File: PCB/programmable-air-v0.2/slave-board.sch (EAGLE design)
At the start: 20 parts, among them Q1 600mA/40V, Q2 600mA/40V, Q3 600mA/40V

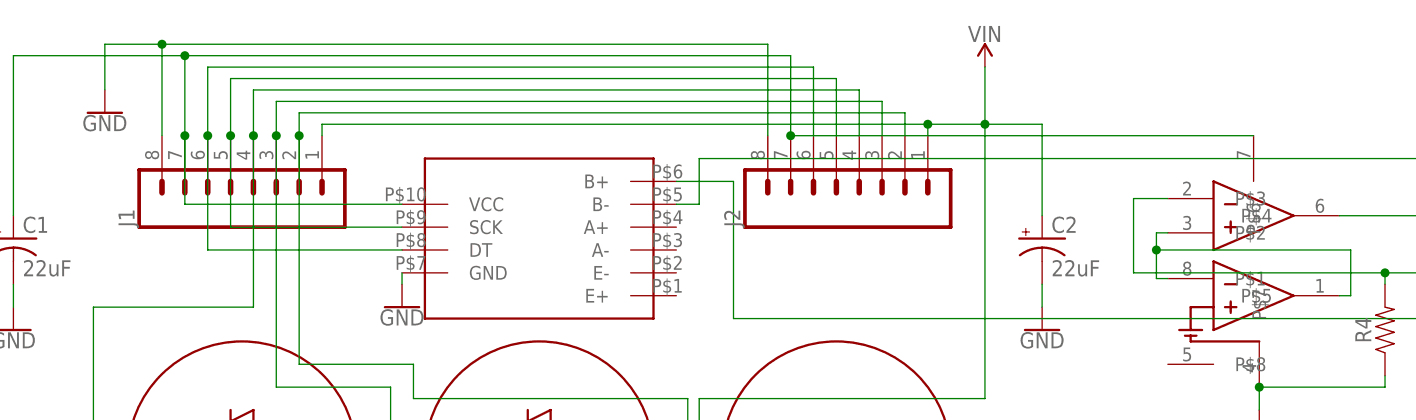
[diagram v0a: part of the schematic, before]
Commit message: PCB v0.2 slave board ready
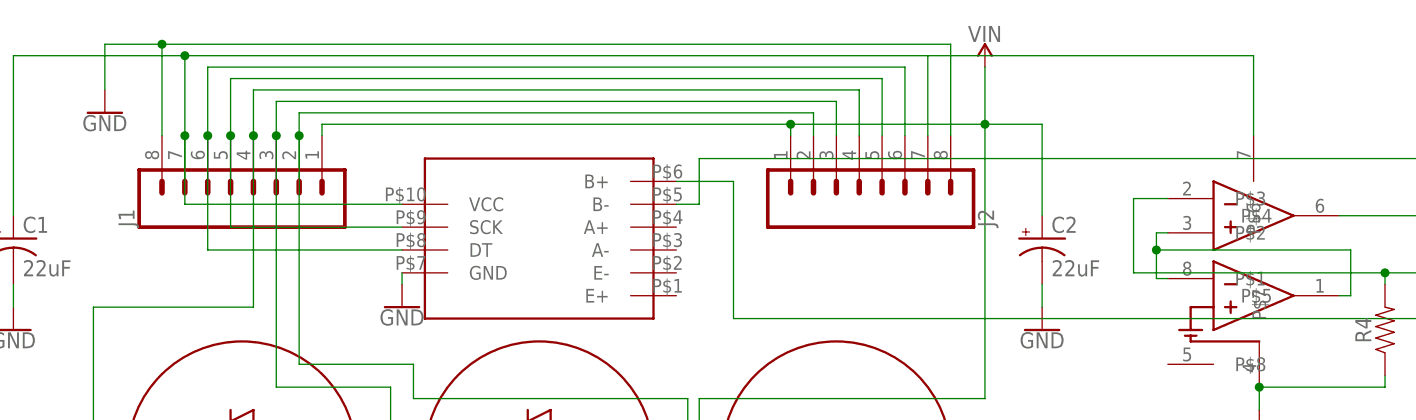
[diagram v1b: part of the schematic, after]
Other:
- moved on the sheet: J2
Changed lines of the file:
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@@
 <?xml version="1.0" encoding="utf-8"?>
 <!DOCTYPE eagle SYSTEM "eagle.dtd">
-<eagle version="8.2.1">
+<eagle version="8.7.0">
 <drawing>
 <settings>
 <setting alwaysvectorfont="no"/>
+<setting keepoldvectorfont="yes"/>
 <setting verticaltext="up"/>
 </settings>
-<grid distance="0.1" unitdist="inch" unit="inch" style="lines" multiple="1" display="no" altdistance="0.01" altunitdist="inch" altunit="inch"/>
+<grid distance="0.05" unitdist="inch" unit="inch" style="lines" multiple="1" display="no" altdistance="0.01" altunitdist="inch" altunit="inch"/>
 <layers>
 <layer number="1" name="Top" color="4" fill="1" visible="no" active="no"/>
@@
 <instance part="U$4" gate="G$1" x="33.02" y="-10.16"/>
 <instance part="J1" gate="G$1" x="-31.75" y="20.32" rot="R90"/>
-<instance part="J2" gate="G$1" x="35.56" y="20.32" rot="R90"/>
+<instance part="J2" gate="G$1" x="35.56" y="20.32" rot="MR90"/>
 <instance part="Q1" gate="G$1" x="-35.56" y="-16.51"/>
 <instance part="Q2" gate="G$1" x="-2.54" y="-16.51"/>
@@
 <net name="N$5" class="0">
 <segment>
-<pinref part="J2" gate="G$1" pin="2"/>
-<wire x1="40.64" y1="25.4" x2="40.64" y2="27.94" width="0.1524" layer="91"/>
-<wire x1="40.64" y1="27.94" x2="-26.67" y2="27.94" width="0.1524" layer="91"/>
 <pinref part="J1" gate="G$1" pin="2"/>
 <wire x1="-26.67" y1="27.94" x2="-26.67" y2="25.4" width="0.1524" layer="91"/>
@@
 <wire x1="-26.67" y1="0" x2="-26.67" y2="25.4" width="0.1524" layer="91"/>
 <junction x="-26.67" y="25.4"/>
+<pinref part="J2" gate="G$1" pin="2"/>
+<wire x1="30.48" y1="25.4" x2="30.48" y2="27.94" width="0.1524" layer="91"/>
+<wire x1="30.48" y1="27.94" x2="-26.67" y2="27.94" width="0.1524" layer="91"/>
 </segment>
 </net>
@@
 <pinref part="J1" gate="G$1" pin="3"/>
 <wire x1="-29.21" y1="25.4" x2="-29.21" y2="29.21" width="0.1524" layer="91"/>
-<wire x1="-29.21" y1="29.21" x2="38.1" y2="29.21" width="0.1524" layer="91"/>
-<pinref part="J2" gate="G$1" pin="3"/>
-<wire x1="38.1" y1="29.21" x2="38.1" y2="25.4" width="0.1524" layer="91"/>
 <wire x1="-29.21" y1="25.4" x2="-29.21" y2="-2.54" width="0.1524" layer="91"/>
 <wire x1="-29.21" y1="-2.54" x2="-16.51" y2="-2.54" width="0.1524" layer="91"/>
@@
 <wire x1="-16.51" y1="-2.54" x2="-16.51" y2="-16.51" width="0.1524" layer="91"/>
 <junction x="-29.21" y="25.4"/>
+<wire x1="-29.21" y1="29.21" x2="33.02" y2="29.21" width="0.1524" layer="91"/>
+<pinref part="J2" gate="G$1" pin="3"/>
+<wire x1="33.02" y1="29.21" x2="33.02" y2="25.4" width="0.1524" layer="91"/>
 </segment>
 </net>
 <net name="N$12" class="0">
 <segment>
-<pinref part="J2" gate="G$1" pin="4"/>
-<wire x1="35.56" y1="25.4" x2="35.56" y2="30.48" width="0.1524" layer="91"/>
-<wire x1="35.56" y1="30.48" x2="-31.75" y2="30.48" width="0.1524" layer="91"/>
 <pinref part="J1" gate="G$1" pin="4"/>
 <wire x1="-31.75" y1="30.48" x2="-31.75" y2="25.4" width="0.1524" layer="91"/>
@@
 <wire x1="-31.75" y1="6.35" x2="-31.75" y2="25.4" width="0.1524" layer="91"/>
 <junction x="-31.75" y="25.4"/>
+<pinref part="J2" gate="G$1" pin="4"/>
+<wire x1="35.56" y1="25.4" x2="35.56" y2="30.48" width="0.1524" layer="91"/>
+<wire x1="35.56" y1="30.48" x2="-31.75" y2="30.48" width="0.1524" layer="91"/>
 </segment>
 </net>
@@
 <pinref part="J1" gate="G$1" pin="5"/>
 <wire x1="-34.29" y1="25.4" x2="-34.29" y2="31.75" width="0.1524" layer="91"/>
-<wire x1="-34.29" y1="31.75" x2="33.02" y2="31.75" width="0.1524" layer="91"/>
-<pinref part="J2" gate="G$1" pin="5"/>
-<wire x1="33.02" y1="31.75" x2="33.02" y2="25.4" width="0.1524" layer="91"/>
 <pinref part="U$1" gate="G$1" pin="SCK"/>
 <wire x1="-34.29" y1="25.4" x2="-34.29" y2="15.24" width="0.1524" layer="91"/>
 <wire x1="-34.29" y1="15.24" x2="-15.24" y2="15.24" width="0.1524" layer="91"/>
 <junction x="-34.29" y="25.4"/>
+<pinref part="J2" gate="G$1" pin="5"/>
+<wire x1="-34.29" y1="31.75" x2="38.1" y2="31.75" width="0.1524" layer="91"/>
+<wire x1="38.1" y1="31.75" x2="38.1" y2="25.4" width="0.1524" layer="91"/>
 </segment>
 </net>
 <net name="N$14" class="0">
 <segment>
-<pinref part="J2" gate="G$1" pin="6"/>
-<wire x1="30.48" y1="25.4" x2="30.48" y2="33.02" width="0.1524" layer="91"/>
-<wire x1="30.48" y1="33.02" x2="-36.83" y2="33.02" width="0.1524" layer="91"/>
 <pinref part="J1" gate="G$1" pin="6"/>
 <wire x1="-36.83" y1="33.02" x2="-36.83" y2="25.4" width="0.1524" layer="91"/>
@@
 <wire x1="-36.83" y1="12.7" x2="-36.83" y2="25.4" width="0.1524" layer="91"/>
 <junction x="-36.83" y="25.4"/>
+<pinref part="J2" gate="G$1" pin="6"/>
+<wire x1="40.64" y1="25.4" x2="40.64" y2="33.02" width="0.1524" layer="91"/>
+<wire x1="40.64" y1="33.02" x2="-36.83" y2="33.02" width="0.1524" layer="91"/>
 </segment>
 </net>
@@
 <pinref part="J1" gate="G$1" pin="7"/>
 <wire x1="-39.37" y1="25.4" x2="-39.37" y2="34.29" width="0.1524" layer="91"/>
-<wire x1="-39.37" y1="34.29" x2="27.94" y2="34.29" width="0.1524" layer="91"/>
-<pinref part="J2" gate="G$1" pin="7"/>
-<wire x1="27.94" y1="34.29" x2="27.94" y2="25.4" width="0.1524" layer="91"/>
 <pinref part="U$1" gate="G$1" pin="VCC"/>
 <wire x1="-39.37" y1="25.4" x2="-39.37" y2="17.78" width="0.1524" layer="91"/>
@@
 <wire x1="-39.37" y1="34.29" x2="-58.42" y2="34.29" width="0.1524" layer="91"/>
 <wire x1="-58.42" y1="34.29" x2="-58.42" y2="16.51" width="0.1524" layer="91"/>
+<junction x="-39.37" y="25.4"/>
+<pinref part="J2" gate="G$1" pin="7"/>
+<wire x1="-39.37" y1="34.29" x2="43.18" y2="34.29" width="0.1524" layer="91"/>
 <junction x="-39.37" y="34.29"/>
-<junction x="-39.37" y="25.4"/>
+<wire x1="43.18" y1="34.29" x2="43.18" y2="25.4" width="0.1524" layer="91"/>
 <pinref part="U$9" gate="G$1" pin="P$6"/>
-<wire x1="27.94" y1="25.4" x2="79.375" y2="25.4" width="0.1524" layer="91"/>
-<junction x="27.94" y="25.4"/>
+<wire x1="43.18" y1="34.29" x2="79.375" y2="34.29" width="0.1524" layer="91"/>
+<wire x1="79.375" y1="34.29" x2="79.375" y2="25.4" width="0.1524" layer="91"/>
 </segment>
 </net>
@@
 <pinref part="J1" gate="G$1" pin="1"/>
 <wire x1="-24.13" y1="25.4" x2="-24.13" y2="26.67" width="0.1524" layer="91"/>
-<pinref part="J2" gate="G$1" pin="1"/>
-<wire x1="-24.13" y1="26.67" x2="43.18" y2="26.67" width="0.1524" layer="91"/>
-<wire x1="43.18" y1="26.67" x2="43.18" y2="25.4" width="0.1524" layer="91"/>
+<wire x1="-24.13" y1="26.67" x2="27.94" y2="26.67" width="0.1524" layer="91"/>
 <pinref part="SUPPLY1" gate="G$1" pin="VIN"/>
-<wire x1="43.18" y1="26.67" x2="49.53" y2="26.67" width="0.1524" layer="91"/>
+<wire x1="27.94" y1="26.67" x2="49.53" y2="26.67" width="0.1524" layer="91"/>
 <wire x1="49.53" y1="26.67" x2="49.53" y2="33.02" width="0.1524" layer="91"/>
 <pinref part="U$2" gate="G$1" pin="P$1"/>
@@
 <junction x="17.78" y="-7.62"/>
 <junction x="-15.24" y="-8.89"/>
-<junction x="43.18" y="26.67"/>
 <junction x="17.78" y="-8.89"/>
 <pinref part="C2" gate="G$1" pin="+"/>
 <wire x1="55.88" y1="16.51" x2="55.88" y2="26.67" width="0.1524" layer="91"/>
 <wire x1="49.53" y1="26.67" x2="55.88" y2="26.67" width="0.1524" layer="91"/>
+<pinref part="J2" gate="G$1" pin="1"/>
+<wire x1="27.94" y1="26.67" x2="27.94" y2="25.4" width="0.1524" layer="91"/>
+<junction x="27.94" y="26.67"/>
 </segment>
 </net>
@@
 <wire x1="-48.26" y1="35.56" x2="-41.91" y2="35.56" width="0.1524" layer="91"/>
 <pinref part="J1" gate="G$1" pin="8"/>
+<wire x1="-41.91" y1="35.56" x2="-41.91" y2="25.4" width="0.1524" layer="91"/>
 <pinref part="J2" gate="G$1" pin="8"/>
-<wire x1="25.4" y1="25.4" x2="25.4" y2="35.56" width="0.1524" layer="91"/>
-<wire x1="25.4" y1="35.56" x2="-41.91" y2="35.56" width="0.1524" layer="91"/>
-<wire x1="-41.91" y1="35.56" x2="-41.91" y2="25.4" width="0.1524" layer="91"/>
+<wire x1="45.72" y1="25.4" x2="45.72" y2="35.56" width="0.1524" layer="91"/>
+<wire x1="45.72" y1="35.56" x2="-41.91" y2="35.56" width="0.1524" layer="91"/>
 <junction x="-41.91" y="35.56"/>
 </segment>

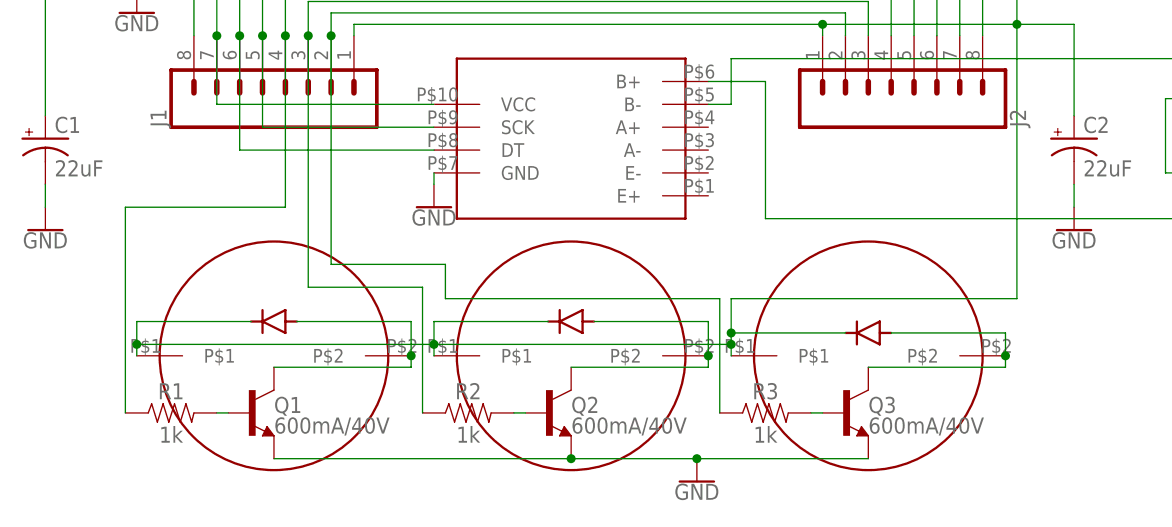
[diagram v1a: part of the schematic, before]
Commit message: Minor fixes to slave PCB after assembly. Started work on test code for PCB v0.2
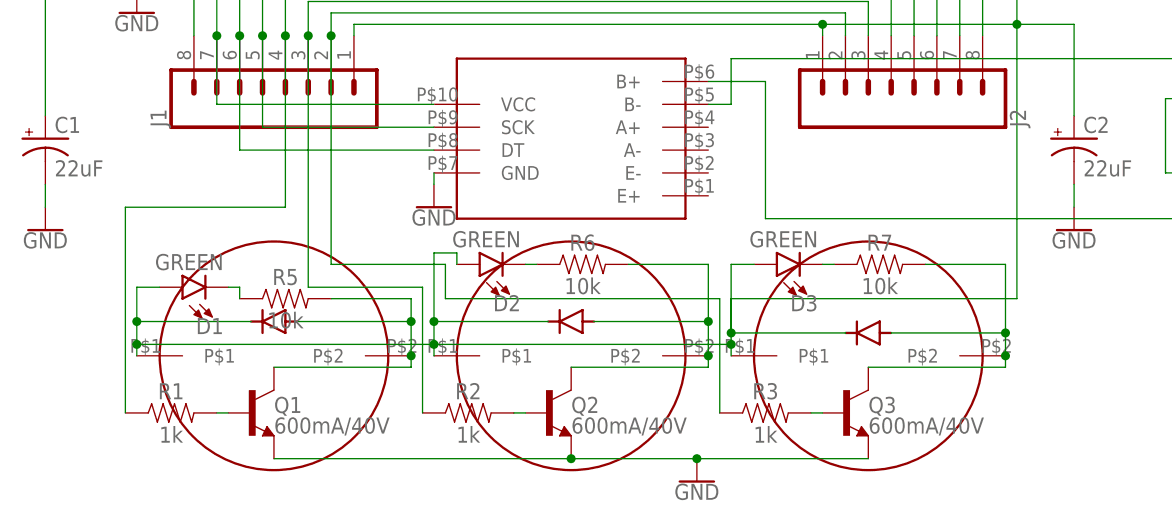
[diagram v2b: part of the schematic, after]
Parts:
- added D1, D2, D3: GREEN, SparkFun-LED:LED-GREEN0603
- added R5, R6, R7: 10k, SparkFun-Resistors:10KOHM-0603-1/10W-1%
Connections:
- new net N$11: D2.C, R6.1
- new net N$18: D1.C, R5.1
- new net N$6: D3.C, R7.1
- net N$7: now also R7.2
- net N$8: now also R6.2
- net N$9: now also R5.2
- net VIN: now also D1.A, D2.A, D3.A
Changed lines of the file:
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@@
 <part name="R4" library="SparkFun-Resistors" deviceset="RESISTOR" device="AXIAL-0.3" value=" "/>
 <part name="GND6" library="SparkFun-PowerSymbols" deviceset="GND" device=""/>
+<part name="D1" library="SparkFun-LED" deviceset="LED-GREEN" device="0603" value="GREEN"/>
+<part name="D2" library="SparkFun-LED" deviceset="LED-GREEN" device="0603" value="GREEN"/>
+<part name="D3" library="SparkFun-LED" deviceset="LED-GREEN" device="0603" value="GREEN"/>
+<part name="R5" library="SparkFun-Resistors" deviceset="10KOHM" device="-0603-1/10W-1%" value="10k"/>
+<part name="R6" library="SparkFun-Resistors" deviceset="10KOHM" device="-0603-1/10W-1%" value="10k"/>
+<part name="R7" library="SparkFun-Resistors" deviceset="10KOHM" device="-0603-1/10W-1%" value="10k"/>
 </parts>
 <sheets>
@@
 <instance part="R4" gate="G$1" x="93.98" y="3.81" rot="R90"/>
 <instance part="GND6" gate="1" x="80.01" y="-7.62"/>
+<instance part="D1" gate="G$1" x="-43.18" y="-2.54" rot="R90"/>
+<instance part="D2" gate="G$1" x="-10.16" y="0" rot="R90"/>
+<instance part="D3" gate="G$1" x="22.86" y="0" rot="R90"/>
+<instance part="R5" gate="G$1" x="-31.75" y="-3.81"/>
+<instance part="R6" gate="G$1" x="1.27" y="0"/>
+<instance part="R7" gate="G$1" x="34.29" y="0"/>
 </instances>
 <busses>
@@
 <wire x1="48.26" y1="-7.62" x2="48.26" y2="-10.16" width="0.1524" layer="91"/>
 <junction x="48.26" y="-10.16"/>
+<pinref part="R7" gate="G$1" pin="2"/>
+<wire x1="39.37" y1="0" x2="48.26" y2="0" width="0.1524" layer="91"/>
+<wire x1="48.26" y1="0" x2="48.26" y2="-7.62" width="0.1524" layer="91"/>
+<junction x="48.26" y="-7.62"/>
 </segment>
 </net>
@@
 <wire x1="15.24" y1="-6.35" x2="15.24" y2="-10.16" width="0.1524" layer="91"/>
 <junction x="15.24" y="-10.16"/>
+<pinref part="R6" gate="G$1" pin="2"/>
+<wire x1="6.35" y1="0" x2="15.24" y2="0" width="0.1524" layer="91"/>
+<wire x1="15.24" y1="0" x2="15.24" y2="-6.35" width="0.1524" layer="91"/>
+<junction x="15.24" y="-6.35"/>
 </segment>
 </net>
@@
 <wire x1="-17.78" y1="-6.35" x2="-17.78" y2="-10.16" width="0.1524" layer="91"/>
 <junction x="-17.78" y="-10.16"/>
+<pinref part="R5" gate="G$1" pin="2"/>
+<wire x1="-26.67" y1="-3.81" x2="-17.78" y2="-3.81" width="0.1524" layer="91"/>
+<wire x1="-17.78" y1="-3.81" x2="-17.78" y2="-6.35" width="0.1524" layer="91"/>
+<junction x="-17.78" y="-6.35"/>
 </segment>
 </net>
@@
 <wire x1="27.94" y1="26.67" x2="27.94" y2="25.4" width="0.1524" layer="91"/>
 <junction x="27.94" y="26.67"/>
+<wire x1="17.78" y1="-7.62" x2="17.78" y2="0" width="0.1524" layer="91"/>
+<pinref part="D3" gate="G$1" pin="A"/>
+<wire x1="17.78" y1="0" x2="20.32" y2="0" width="0.1524" layer="91"/>
+<wire x1="-15.24" y1="-6.35" x2="-15.24" y2="1.27" width="0.1524" layer="91"/>
+<junction x="-15.24" y="-6.35"/>
+<wire x1="-15.24" y1="1.27" x2="-12.7" y2="1.27" width="0.1524" layer="91"/>
+<pinref part="D2" gate="G$1" pin="A"/>
+<wire x1="-12.7" y1="1.27" x2="-12.7" y2="0" width="0.1524" layer="91"/>
+<pinref part="D1" gate="G$1" pin="A"/>
+<wire x1="-48.26" y1="-6.35" x2="-48.26" y2="-2.54" width="0.1524" layer="91"/>
+<wire x1="-48.26" y1="-2.54" x2="-45.72" y2="-2.54" width="0.1524" layer="91"/>
+<junction x="-48.26" y="-6.35"/>
 </segment>
 </net>
@@
 </segment>
 </net>
+<net name="N$6" class="0">
+<segment>
+<pinref part="D3" gate="G$1" pin="C"/>
+<pinref part="R7" gate="G$1" pin="1"/>
+<wire x1="27.94" y1="0" x2="29.21" y2="0" width="0.1524" layer="91"/>
+</segment>
+</net>
+<net name="N$11" class="0">
+<segment>
+<pinref part="D2" gate="G$1" pin="C"/>
+<pinref part="R6" gate="G$1" pin="1"/>
+<wire x1="-5.08" y1="0" x2="-3.81" y2="0" width="0.1524" layer="91"/>
+</segment>
+</net>
+<net name="N$18" class="0">
+<segment>
+<pinref part="D1" gate="G$1" pin="C"/>
+<pinref part="R5" gate="G$1" pin="1"/>
+<wire x1="-38.1" y1="-2.54" x2="-36.83" y2="-2.54" width="0.1524" layer="91"/>
+<wire x1="-36.83" y1="-2.54" x2="-36.83" y2="-3.81" width="0.1524" layer="91"/>
+</segment>
+</net>

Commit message: LM358 slave board ready
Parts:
- removed R4: (no value), SparkFun-Resistors:RESISTORAXIAL-0.3
- added IC1: INA126U, INA126:INA126U
- added IC3: LM358MX, linear:LM358MX
- added R10: 1.78K, eagle-ltspice:RR0603
- added R13, R14, R15, R8, R9: 10K, eagle-ltspice:RR0603
- added R16: 40K, eagle-ltspice:RR0603
- added R17, R20: 20K, eagle-ltspice:RR0603
- added U$10: BUTTON, programmable-air-components:BUTTON
- U$1: value HX711 -> 2SMPP-03; device programmable-air-components:HX711 -> programmable-air-components:2SMPP-03
- U$8: value 2SMPP-03 -> BUTTON; device programmable-air-components:2SMPP-03 -> programmable-air-components:BUTTON
- U$9: value LM10CN -> BUTTON; device programmable-air-components:LM10CN -> programmable-air-components:BUTTON
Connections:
- removed net N$16: U$8.5, U$8.6, U$9.P$4
- removed net N$17: R4.2, U$8.3, U$9.P$3
- removed net N$21: U$1.B+, U$8.1
- removed net N$22: U$1.B-, U$8.4
- new net N$19: IC3A.OUT, U$1.5, U$1.6
- new net N$20: IC1.+IN, U$1.4
- new net N$24: IC3A.+IN, R16.1, R8.2
- new net N$25: IC1.RG@1, R10.1
- new net N$26: IC1.RG, R10.2
- new net N$27: IC3B.-IN, R13.2, R17.2, R20.1
- new net N$30: IC3B.+IN, R14.2, R15.1
- new net N$31: IC3A.-IN, R9.2, U$1.3
- net GND: now also IC1.V-, IC3P.V-, R14.1, R17.1, R8.1, R9.1; no longer R4.1, U$1.GND, U$9.P$7
- net N$1: now also U$8.P$2
- net N$13: now also IC3B.OUT, R13.1; no longer U$1.SCK
- net N$14: no longer U$1.DT
- net N$15: now also IC1.REF, IC3P.V+, R15.2, R16.2, R20.2, U$10.P$1, U$8.P$1, U$9.P$1; no longer U$1.VCC, U$9.P$6
- net N$2: now also U$9.P$2
- net N$3: now also U$10.P$2
- net N$4: now also IC1.-IN, U$1.1; no longer U$9.P$1, U$9.P$2, U$9.P$5
- net VIN: now also IC1.V+
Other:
- note added: "Precision"
- moved on the sheet: C2

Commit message: LM358 slave board final
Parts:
- removed R10: 1.78K, eagle-ltspice:RR0603
- removed R13, R14, R15, R8, R9: 10K, eagle-ltspice:RR0603
- removed R16: 40K, eagle-ltspice:RR0603
- removed R17, R20: 20K, eagle-ltspice:RR0603
- added R11, R12, R18, R19, R4: 10k, SparkFun-Resistors:10KOHM-0603-1/10W-1%
- added R21: 40K, SparkFun-Resistors:10KOHM-0603-1/10W-1%
- added R22, R23: 20K, SparkFun-Resistors:10KOHM-0603-1/10W-1%
- added R24: 2K, SparkFun-Resistors:10KOHM-0603-1/10W-1%
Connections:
- new net N$16: IC1.OUT, R22.1
- net GND: now also R11.1, R12.1, R23.1, R4.1; no longer R14.1, R17.1, R8.1, R9.1
- net N$13: now also R19.1; no longer R13.1
- net N$15: now also R18.2, R21.1; no longer R15.2, R16.2, R20.2
- net N$24: now also R21.2, R4.2; no longer R16.1, R8.2
- net N$25: now also R24.1; no longer R10.1
- net N$26: now also R24.2; no longer R10.2
- net N$27: now also R19.2, R22.2, R23.2; no longer R13.2, R17.2, R20.1
- net N$30: now also R12.2, R18.1; no longer R14.2, R15.1
- net N$31: now also R11.2; no longer R9.2
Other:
- moved on the sheet: IC1, IC3A, IC3B
